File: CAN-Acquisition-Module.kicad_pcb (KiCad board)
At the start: 4 copper layers, 95 x 65 mm, 214 parts, among them J1 Conn_01x04, J10 OSTVN04A150, J11 OSTVN04A150, J12 OSTVN04A150, J13 OSTVN04A150, J2 Conn_01x02, J3 Conn_01x03, J4 Conn_02x05_Odd_Even, J5 OSTVN04A150, J6 OSTVN04A150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

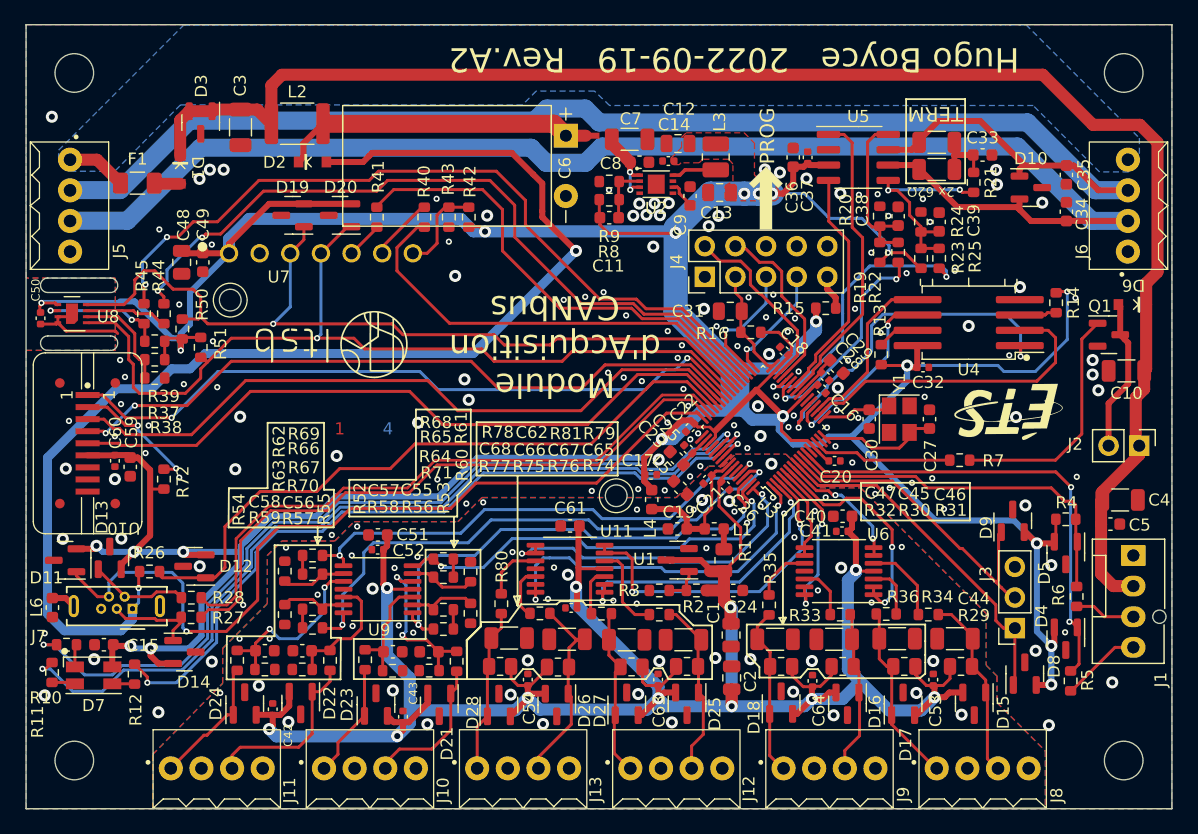
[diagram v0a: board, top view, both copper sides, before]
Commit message: Fixed board and re-exported Gerbers. BOM is a WIP
Some design rules were violated
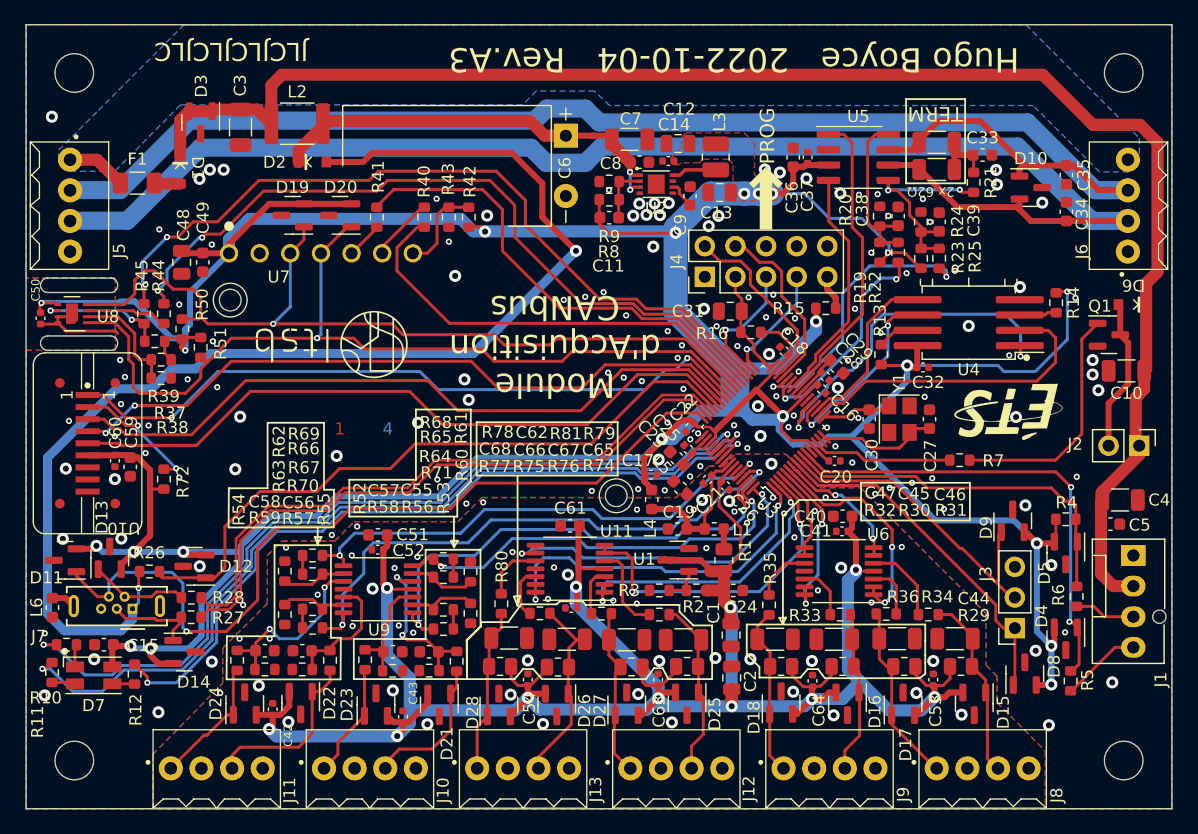
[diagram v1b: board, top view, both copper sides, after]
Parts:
- moved R37 0.53 mm to (31.2, 52.8)
- moved R38 0.53 mm to (31.2, 54.3)
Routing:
- net Net-(C6-Pad1): track 0.00 -> 26.3 mm
- net Net-(C7-Pad1): track 32.0 -> 7.29 mm
- net /MCU/SCREEN_CLK: track 58.7 -> 57.9 mm
- net Net-(R37-Pad2): track 8.90 -> 9.47 mm
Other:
- board text added: "Hugo Boyce 2022-10-04 Rev.A3"
- board text added: "JLCJLCJLCJLC"
- board text removed: "Hugo Boyce 2022-09-19 Rev.A2"

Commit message: Created Rev B1
Replaced buck regulator S-8581AA with AP63200 because of shortage
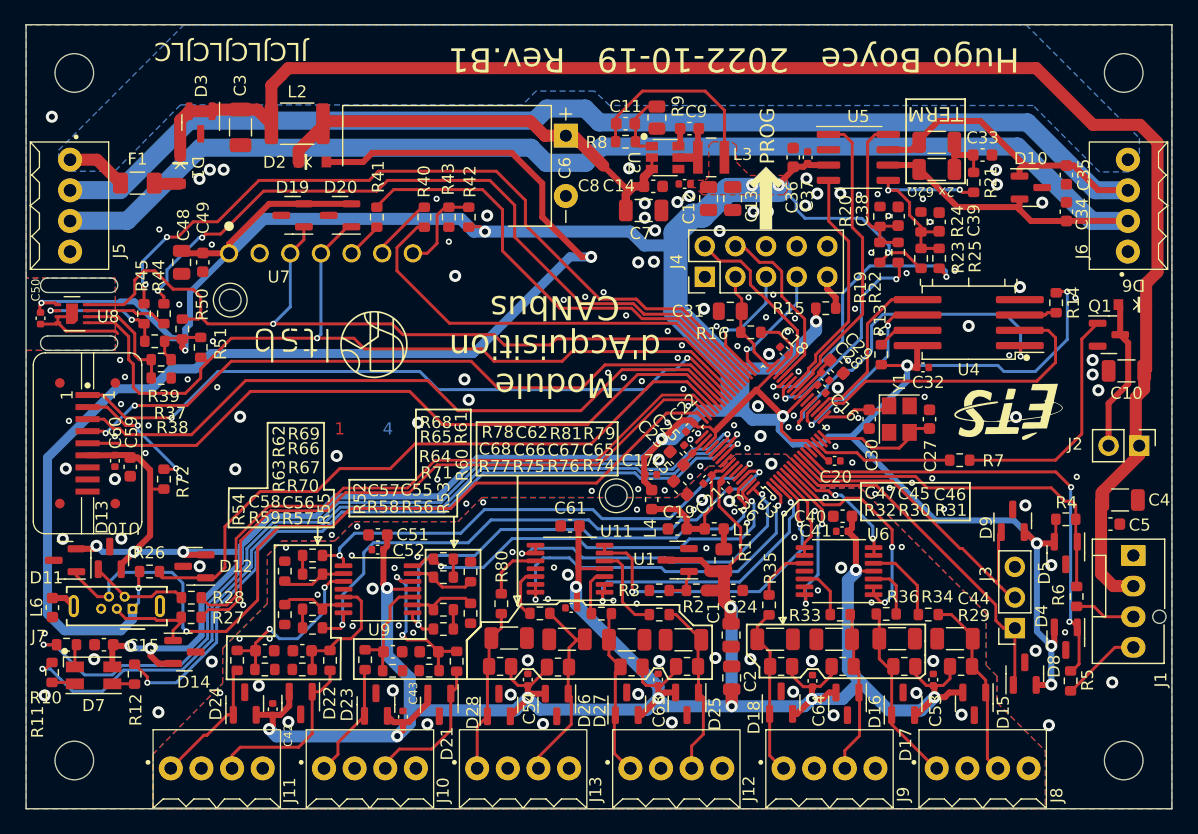
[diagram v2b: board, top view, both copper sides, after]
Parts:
- C11: value 33 pF -> 100 pF
- C44, C45, C46, C47, C65, C66, C67, C68: value 47 uF -> 4.7 uF
- C9: value 1 uF -> 100 nF
- L3: value 4.7 uH -> 6.8 uH; footprint Inductor_SMD:L_1008_2520Metric -> CAN-Acquisition-Module:Murata_LQH3_1212(3030_Metric)
- R20: value 22 kΩ -> 18.2 kΩ
- R8: value 47 kΩ -> 18.2 kΩ
- R9: value 15 kΩ -> 6.2 kΩ; footprint Resistor_SMD:R_0603_1608Metric -> Resistor_SMD:R_0805_2012Metric
- U2: value S-8581AA -> AP63200; footprint CAN-Acquisition-Module:Ablic_HSTN-8-A -> CAN-Acquisition-Module:Diodes-Inc_TSOT26
- U5: value SN65HVD234 -> SN65HVD235
- moved C11 7.92 mm to (69.7, 33.2)
- moved R9 6.61 mm to (72.3, 32.7), turned to -90 degrees
- moved C7 6.01 mm to (71.2, 40.4)
- moved C9 5.59 mm to (75.0, 33.6), turned to 180 degrees
- moved NT1 5.47 mm to (70.7, 35.3), turned to -45 degrees
- moved C12 5.22 mm to (76.6, 39.4), turned to -90 degrees
- moved R8 4.99 mm to (69.7, 34.7)
- moved C14 2.33 mm to (74.6, 38.2)
- moved U2 2.33 mm to (73.0, 36.0), turned to -90 degrees
- moved C8 2.30 mm to (72.0, 38.4)
- moved C13 1.20 mm to (78.6, 39.4), turned to -90 degrees
- moved L3 0.38 mm to (76.8, 36.0), turned to 0 degrees
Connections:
- C9 pad 2: GND -> Net-(C9-Pad2)
- L3 pad 1: Net-(L3-Pad1) -> Net-(C9-Pad1)
- U2 pad 1: Net-(C7-Pad1) -> Net-(C11-Pad2)
- U2 pad 2: Net-(C11-Pad2) -> Net-(C7-Pad1)
- U2 pad 4: unconnected-(U2-Pad4) -> GND
- U2 pad 5: unconnected-(U2-Pad5) -> Net-(C9-Pad1)
- U2 pad 6: Net-(C9-Pad1) -> Net-(C9-Pad2)
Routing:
- net +3V3: track 381.6 -> 387.9 mm, vias 21 -> 20
- net Net-(L3-Pad1): track 3.74 -> 0.00 mm
- net Net-(C6-Pad1): track 26.3 -> 28.9 mm
- net /Power/V_USB: track 102.1 -> 104.6 mm
- net Net-(C9-Pad1): track 2.30 -> 4.04 mm
- net Net-(C7-Pad1): track 7.29 -> 5.76 mm, vias 2 -> 0
- net Net-(C9-Pad2): track 0.00 -> 1.51 mm
- net Net-(C11-Pad2): track 4.54 -> 5.66 mm
- net GND: vias 135 -> 136
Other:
- board text added: "Hugo Boyce 2022-10-19 Rev.B1"
- board text removed: "Hugo Boyce 2022-10-04 Rev.A3"

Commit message: Corrected U1 in schematic
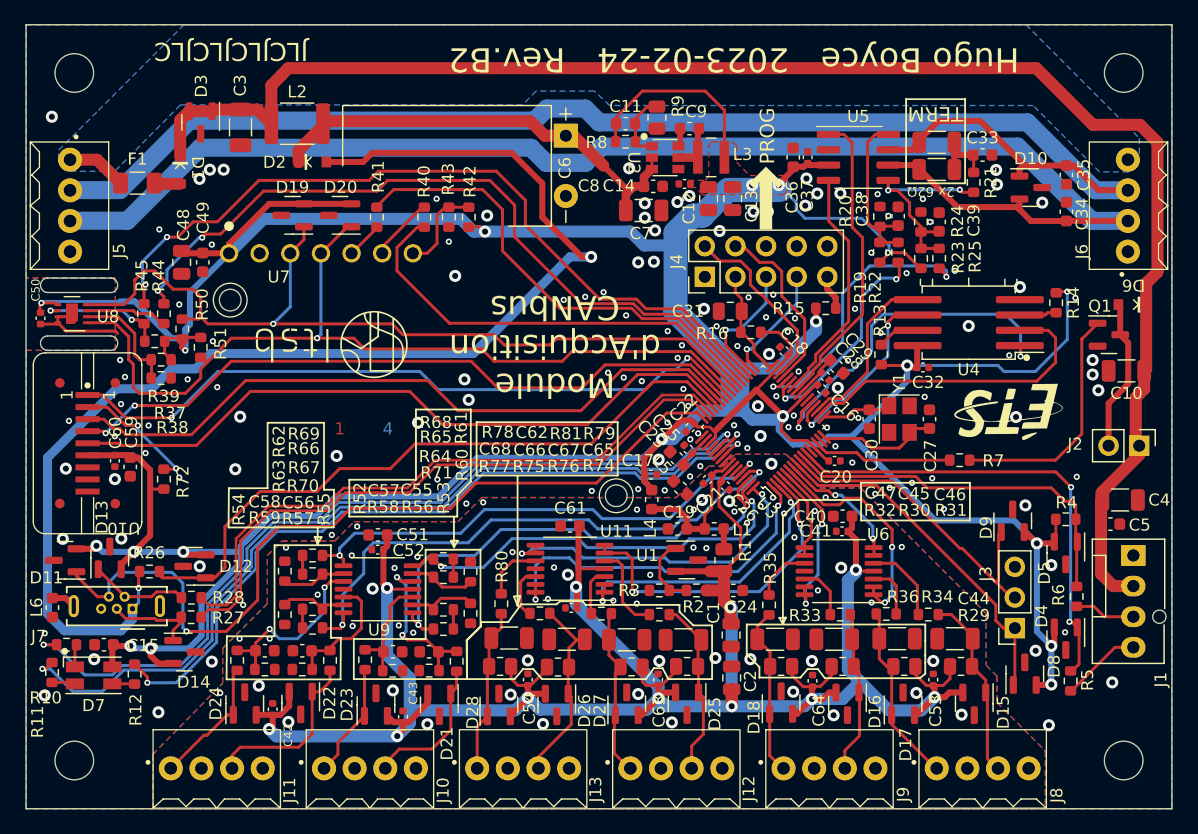
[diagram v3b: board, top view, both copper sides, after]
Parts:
- C11: value 100 pF -> 47 pF
- moved U1 0.77 mm to (74.8, 69.4), turned to 0 degrees
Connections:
- U1 pad 2: GNDA -> +1V8
- U1 pad 3: +1V8 -> GNDA
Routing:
- net Net-(R2-Pad2): track 3.08 -> 6.03 mm
- net +1V8: track 200.5 -> 199.3 mm
- net GNDA: vias 56 -> 58
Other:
- board text added: "Hugo Boyce 2023-02-24 Rev.B2"
- board text removed: "Hugo Boyce 2022-10-19 Rev.B1"
